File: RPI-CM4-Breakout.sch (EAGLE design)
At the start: 27 parts, among them IC1 MC74VHC1G14DFT1G, J1 P1-100, J2 P101-200, J3 47571-0001

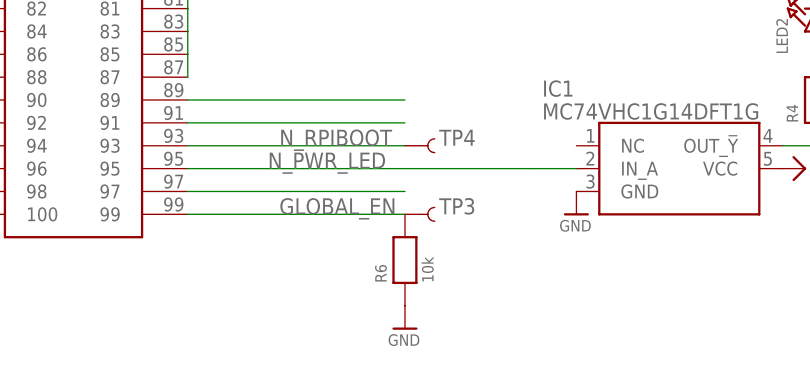
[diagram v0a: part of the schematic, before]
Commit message: Removed misleading pull-down on GLOBAL_EN
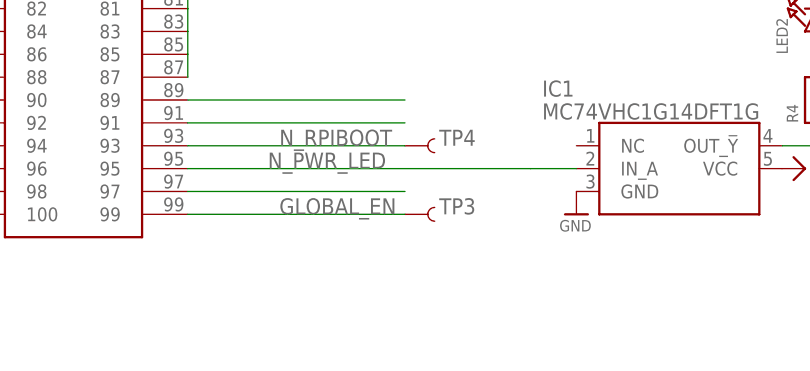
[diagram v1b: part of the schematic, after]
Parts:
- removed R6: 10k, microbuilder:RESISTOR_0402MP
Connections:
- net GLOBAL_EN: no longer R6.2
- net GND: no longer R6.1
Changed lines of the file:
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@@
 <setting verticaltext="up"/>
 </settings>
-<grid distance="0.05" unitdist="inch" unit="inch" style="lines" multiple="1" display="no" altdistance="0.01" altunitdist="inch" altunit="inch"/>
+<grid distance="0.1" unitdist="inch" unit="inch" style="lines" multiple="1" display="no" altdistance="0.01" altunitdist="inch" altunit="inch"/>
 <layers>
 <layer number="1" name="Top" color="4" fill="1" visible="no" active="no"/>
@@
 <part name="TP6" library="SparkFun-Connectors" deviceset="TEST-POINT" device="3X5"/>
 <part name="TP7" library="SparkFun-Connectors" deviceset="TEST-POINT" device="3X5"/>
-<part name="R6" library="microbuilder" deviceset="RESISTOR" device="_0402MP" value="10k"/>
-<part name="U$68" library="microbuilder" deviceset="GND" device=""/>
 <part name="C2" library="microbuilder" deviceset="CAP_CERAMIC" device="0402"/>
 <part name="C3" library="microbuilder" deviceset="CAP_CERAMIC" device="0402"/>
@@
 <attribute name="NAME" x="78.74" y="71.12" size="1.778" layer="95" font="vector"/>
 </instance>
-<instance part="R6" gate="G$1" x="74.93" y="10.16" smashed="yes" rot="R90">
-<attribute name="NAME" x="72.898" y="7.62" size="1.27" layer="95" font="vector" rot="R90"/>
-<attribute name="VALUE" x="78.105" y="7.62" size="1.27" layer="96" font="vector" rot="R90"/>
-</instance>
-<instance part="U$68" gate="G$1" x="74.93" y="2.54" smashed="yes">
-<attribute name="VALUE" x="73.025" y="0.635" size="1.27" layer="96"/>
-</instance>
 <instance part="C2" gate="G$1" x="115.57" y="210.82" smashed="yes">
 <attribute name="NAME" x="118.11" y="213.36" size="1.27" layer="95" font="vector"/>
@@
 <label x="60.96" y="15.24" size="1.778" layer="95"/>
 <pinref part="TP3" gate="G$1" pin="1"/>
-<pinref part="R6" gate="G$1" pin="2"/>
 </segment>
 </net>
@@
 </segment>
 <segment>
-<pinref part="R6" gate="G$1" pin="1"/>
-<pinref part="U$68" gate="G$1" pin="GND"/>
-</segment>
-<segment>
